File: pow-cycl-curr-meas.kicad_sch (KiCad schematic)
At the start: 86 parts, among them Q10 2N7002K-T1-E3, Q6 2N7002K-T1-E3, Q7 2N7002K-T1-E3, Q8 2N7002K-T1-E3, Q9 2N7002K-T1-E3, U10 TCA9534, U11 TMCS1100A2-Q1, U12 TMCS1100A2-Q1, U13 TMCS1100A2-Q1, U14 ADS7828, U8 TMCS1100A2-Q1, U9 TMCS1100A2-Q1

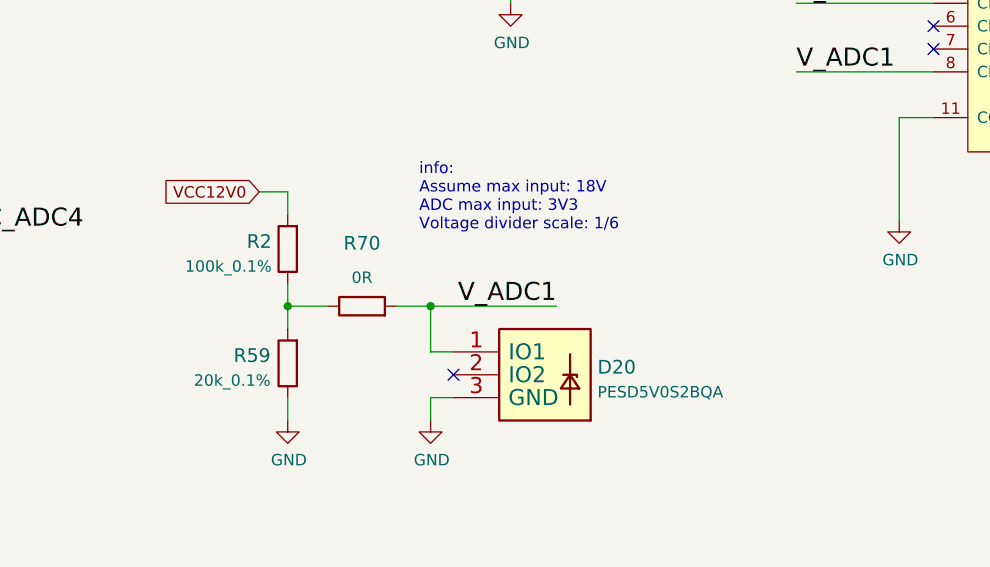
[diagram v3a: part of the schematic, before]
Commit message: Exchanged resistor in divider for voltage measurement
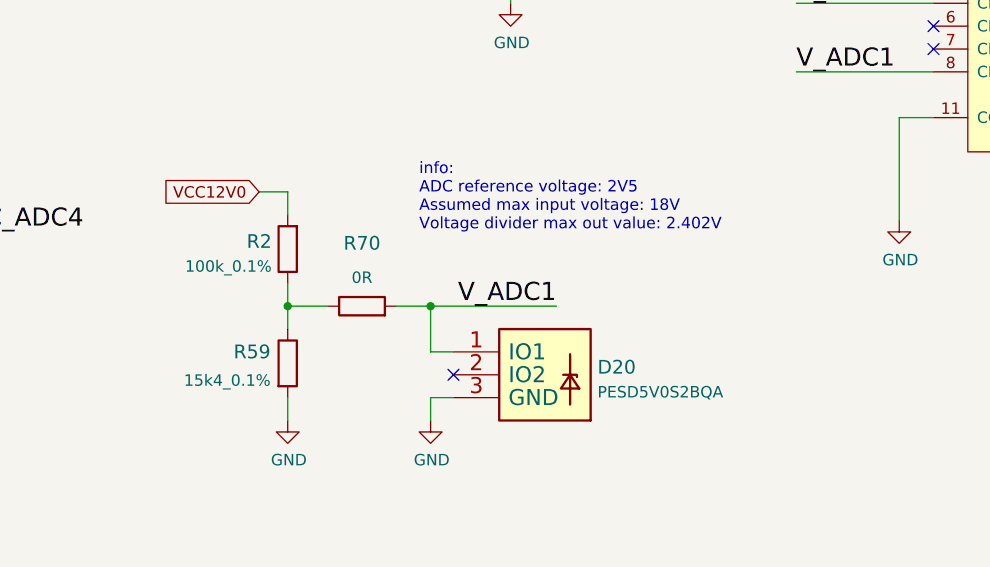
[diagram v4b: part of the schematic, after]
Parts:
- removed R59: R_20k_0.1%_0402, antmicro-footprints:0402-res, symbol antmicroResistors0402:R_20k_0.1%_0402
- added R59: R_15k4_0.1%_0402, antmicro-footprints:0402-res, symbol antmicroResistors0402:R_15k4_0.1%_0402
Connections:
- net GND: now also R59.2
- net at R2.1, R70.1: now also R59.1
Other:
- note added: "info: ADC reference voltage: 2V5 Assumed max input voltage: 18V Voltage divider max out value: 2.402V"
- note removed: "info: Assume max input: 18V ADC max input: 3V3 Voltage divider scale: 1/6"
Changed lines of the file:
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@@
     (effects (font (size 2.0066 2.0066)) (justify left bottom))
   )
-  (text "info:\nAssume max input: 18V\nADC max input: 3V3\nVoltage divider scale: 1/6"
+  (text "info:\nADC reference voltage: 2V5\nAssumed max input voltage: 18V\nVoltage divider max out value: 2.402V"
     (at 196.85 91.44 0)
     (effects (font (size 1.27 1.27)) (justify left bottom))
@@
     (pin "1")
   )
+  (symbol (lib_id "antmicroResistors0402:R_15k4_0.1%_0402") (at 182.245 106.045 270) (unit 1)
+    (in_bom yes) (on_board yes)
+    (property "Reference" "R59" (id 0) (at 180.34 104.7751 90)
+      (effects (font (size 1.524 1.524)) (justify right))
+    )
+    (property "Value" "R_15k4_0.1%_0402" (id 1) (at 174.625 106.045 0)
+      (effects (font (size 1.524 1.524)) hide)
+    )
+    (property "Footprint" "antmicro-footprints:0402-res" (id 2) (at 187.325 111.125 0)
+      (effects (font (size 1.524 1.524)) (justify left) hide)
+    )
+    (property "Datasheet" "https://www.mouser.pl/datasheet/2/315/AOA0000C307-1149632.pdf" (id 3) (at 177.165 106.045 0)
+      (effects (font (size 1.27 1.27)) hide)
+    )
+    (property "Manufacturer" "Panasonic" (id 4) (at 192.405 111.125 0)
+      (effects (font (size 1.524 1.524)) (justify left) hide)
+    )
+    (property "MPN" "ERA-2AEB1542X" (id 5) (at 189.865 111.125 0)
+      (effects (font (size 1.524 1.524)) (justify left) hide)
+    )
+    (property "Val" "15k4_0.1%" (id 6) (at 180.34 107.95 90)
+      (effects (font (size 1.27 1.27)) (justify right))
+    )
+    (pin "1")
+    (pin "2")
+  )
   (symbol (lib_id "antmicroTransistorsFETsMOSFETsSingle:2N7002K-T1-E3") (at 246.38 247.015 0) (unit 1)
     (in_bom yes) (on_board yes) (fields_autoplaced)
@@
     (pin "3")
   )
-  (symbol (lib_id "antmicroResistors0402:R_20k_0.1%_0402") (at 182.245 106.045 90) (unit 1)
-    (in_bom yes) (on_board yes)
-    (property "Reference" "R59" (id 0) (at 180.34 105.1849 90)
-      (effects (font (size 1.524 1.524)) (justify left))
-    )
-    (property "Value" "R_20k_0.1%_0402" (id 1) (at 187.325 106.045 0)
-      (effects (font (size 1.524 1.524)) hide)
-    )
-    (property "Footprint" "antmicro-footprints:0402-res" (id 2) (at 177.165 100.965 0)
-      (effects (font (size 1.524 1.524)) (justify left) hide)
-    )
-    (property "Datasheet" "https://www.mouser.pl/datasheet/2/447/PYu_RC_Group_51_RoHS_L_11-1984063.pdf" (id 3) (at 189.865 106.045 0)
-      (effects (font (size 1.27 1.27)) hide)
-    )
-    (property "Manufacturer" "Yageo" (id 4) (at 172.085 100.965 0)
-      (effects (font (size 1.524 1.524)) (justify left) hide)
-    )
-    (property "MPN" "RC0402BR-0720KL" (id 5) (at 174.625 100.965 0)
-      (effects (font (size 1.524 1.524)) (justify left) hide)
-    )
-    (property "Val" "20k_0.1%" (id 6) (at 180.34 107.95 90)
-      (effects (font (size 1.27 1.27)) (justify left))
-    )
-    (pin "1")
-    (pin "2")
-  )
   (symbol (lib_id "d1600e-psu-breakout-board:GND") (at 130.175 259.715 0) (unit 1)

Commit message: Fixed IO expander MPN
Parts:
- U10: MPN TCA9534ADWR -> TCA9534PWR
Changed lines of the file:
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@@
       (effects (font (size 1.27 1.27)) hide)
     )
-    (property "MPN" "TCA9534ADWR" (id 4) (at 83.82 185.42 0)
+    (property "MPN" "TCA9534PWR" (id 4) (at 83.82 185.42 0)
       (effects (font (size 1.27 1.27)) hide)
     )

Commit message: [#63472] Add OHP assets
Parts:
- removed C29, C30, C31, C32: C_100n_0402, d1600e-psu-breakout-board-footprints:0402-cap, symbol d1600e-psu-breakout-board:C_100n_0402
- removed D15, D16, D17, D18, D19: BZT52B15SV-T, antmicro-footprints:SOD-323, symbol antmicroDiodesZenerSingle:BZT52B15SV-T
- removed Q10, Q6, Q7, Q8, Q9: 2N7002K-T1-E3, antmicro-footprints:SOT-23-3, symbol antmicroTransistorsFETsMOSFETsSingle:2N7002K-T1-E3
- removed QA1, QA2, QA3, QA4, QA5, QB1, QB2, QB3, QB4, QB5: SI7613DN-T1-GE3, antmicro-footprints:Vishay_PowerPAK_1212-8_Single, symbol antmicroTransistorsFETsMOSFETsSingle:SI7613DN-T1-GE3
- removed R20, R21, R24, R26, R27, R46, R47, R48, R49, R50: R_10k_0402, d1600e-psu-breakout-board-footprints:0402-res, symbol d1600e-psu-breakout-board:R_10k_0402
- removed R22, R23, R25, R28, R29: R_4k7_0402, d1600e-psu-breakout-board-footprints:0402-res, symbol d1600e-psu-breakout-board:R_4k7_0402
- removed R60, R61, R62, R63, R64, R65, R66, R67, R68, R69: R_2R_0402, antmicro-footprints:0402-res, symbol antmicroResistors0402:R_2R_0402
- removed U11, U12, U13, U9: TMCS1100A2-Q1, d1600e-psu-breakout-board-footprints:SOIC-8_W3.9mm, symbol d1600e-psu-breakout-board:TMCS1100A2-Q1
- added C29, C30, C31, C32: C_100n_0402, antmicro-footprints:C_0402_1005Metric, symbol antmicroCapacitors0402:C_100n_0402
- added U11, U12, U13, U9: TMCS1100A2-Q1, antmicro-footprints:SOIC-8_3.9x4.9x1.75mm_P1.27mm, symbol antmicroPowerMeasurement:TMCS1100A2-Q1
- C21, C28, C37: footprint d1600e-psu-breakout-board-footprints:0402-cap -> antmicro-footprints:C_0402_1005Metric; symbol d1600e-psu-breakout-board:C_100n_0402 -> antmicroCapacitors0402:C_100n_0402; Author (none) -> Antmicro; Dielectric (none) -> X5R; License (none) -> Apache-2.0; Voltage (none) -> 50V
- C22: footprint d1600e-psu-breakout-board-footprints:0402-cap -> antmicro-footprints:C_0402_1005Metric; symbol d1600e-psu-breakout-board:C_1u_0402 -> antmicroCapacitors0402:C_1u_0402; Author (none) -> Antmicro; License (none) -> Apache-2.0
- D20: footprint d1600e-psu-breakout-board-footprints:TPD2E009DRTR -> antmicro-footprints:TPD2E009DRTR; symbol d1600e-psu-breakout-board:PESD5V0S2BQA -> antmicroTVSDiodes:PESD5V0S2BQA; Author (none) -> Antmicro; License (none) -> Apache-2.0
- FB4: value BLM18AG601SN1D -> FB_600Z_0.5A_Murata-BLM18AG_0603; footprint d1600e-psu-breakout-board-footprints:0603 -> antmicro-footprints:FB_0603_1608Metric; symbol d1600e-psu-breakout-board:BLM18AG601SN1D -> antmicroFerriteBeadsandChips:FB_600Z_0.5A_Murata-BLM18AG_0603; Author (none) -> Antmicro; DNP DNP -> (none); License (none) -> Apache-2.0; Manufacturer Murata Electronics North America -> Murata; Val (none) -> 600Z/0.5A
- R13, R15, R30, R32: footprint d1600e-psu-breakout-board-footprints:0402-res -> antmicro-footprints:R_0402_1005Metric; symbol d1600e-psu-breakout-board:R_0R_0402 -> antmicroResistors0402:R_0R_0402; Author (none) -> Antmicro; Current (none) -> 1A; License (none) -> Apache-2.0; Manufacturer PANASONIC -> Panasonic; now not fitted; now left out of the parts list
- R14, R16, R18, R31, R33, R70: footprint d1600e-psu-breakout-board-footprints:0402-res -> antmicro-footprints:R_0402_1005Metric; symbol d1600e-psu-breakout-board:R_0R_0402 -> antmicroResistors0402:R_0R_0402; Author (none) -> Antmicro; Current (none) -> 1A; License (none) -> Apache-2.0; Manufacturer PANASONIC -> Panasonic
- R17: footprint d1600e-psu-breakout-board-footprints:0402-res -> antmicro-footprints:R_0402_1005Metric; symbol d1600e-psu-breakout-board:R_0R_0402 -> antmicroResistors0402:R_0R_0402; Author (none) -> Antmicro; Current (none) -> 1A; DNP DNP` -> DNP; License (none) -> Apache-2.0; Manufacturer PANASONIC -> Panasonic; now not fitted; now left out of the parts list
- R19: footprint d1600e-psu-breakout-board-footprints:0402-res -> antmicro-footprints:R_0402_1005Metric; symbol d1600e-psu-breakout-board:R_4k7_0402 -> antmicroResistors0402:R_4k7_0402; Author (none) -> Antmicro; License (none) -> Apache-2.0; MPN MCS04020C4701FE000 -> CR0402-FX-4701GLF; Manufacturer VISHAY -> Bourns; Tolerance (none) -> 1%
- R2: footprint antmicro-footprints:0402-res -> antmicro-footprints:R_0402_1005Metric; Author (none) -> Antmicro; License (none) -> Apache-2.0; Tolerance (none) -> 0.1%; Val 100k_0.1% -> 100k
- R59: footprint antmicro-footprints:0402-res -> antmicro-footprints:R_0402_1005Metric; Author (none) -> Antmicro; License (none) -> Apache-2.0; Tolerance (none) -> 0.1%; Val 15k4_0.1% -> 15k4
- TP_ADC1, TP_ADC2, TP_ADC3, TP_ADC4, TP_ADC5, TP_PC1, TP_PC2, TP_PC3, TP_PC4, TP_PC5: value TP_SMD1MM -> TP_1mm_SMD; footprint d1600e-psu-breakout-board-footprints:Testpoint_smd_1mm -> antmicro-footprints:TP_SMD_1mm; symbol d1600e-psu-breakout-board:TP_SMD1MM -> antmicroTestPoints:TP_1mm_SMD; Author (none) -> Antmicro; License (none) -> Apache-2.0; now left out of the parts list
- U10: value TCA9534 -> TCA9534PWR_TSSOP; footprint d1600e-psu-breakout-board-footprints:TSSOP-16 -> antmicro-footprints:TSSOP-16_4.4x5mm_P0.65mm; symbol d1600e-psu-breakout-board:TCA9534 -> antmicroInterfaceIOExpanders:TCA9534PWR_TSSOP; Author (none) -> Antmicro; License (none) -> Apache-2.0; Manufaacturer Texas Instruments -> (none)
- U14: footprint d1600e-psu-breakout-board-footprints:TSSOP-16_4.4x5mm_P0.65mm -> antmicro-footprints:TSSOP-16_4.4x5mm_P0.65mm; symbol d1600e-psu-breakout-board:ADS7828 -> antmicroDataAcquisitionAnalogtoDigitalConvertersADC:ADS7828; Author (none) -> Antmicro; License (none) -> Apache-2.0; MPN ADS7828E/250 -> ADS7828E/250
- U8: footprint d1600e-psu-breakout-board-footprints:SOIC-8_W3.9mm -> antmicro-footprints:SOIC-8_3.9x4.9x1.75mm_P1.27mm; symbol d1600e-psu-breakout-board:TMCS1100A2-Q1 -> antmicroPowerMeasurement:TMCS1100A2-Q1; Author (none) -> Antmicro; License (none) -> Apache-2.0
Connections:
- net C_ADC2: now also U9.7 (VOUT)
- net C_ADC3: now also U11.7 (VOUT)
- net C_ADC4: now also U12.7 (VOUT)
- net C_ADC5: now also U13.7 (VOUT)
- net C_MEAS_2: now also U9.1 (IN+), U9.2 (IN+)
- net C_MEAS_3: now also U11.1 (IN+), U11.2 (IN+)
- net C_MEAS_4: now also U12.1 (IN+), U12.2 (IN+)
- net C_MEAS_5: now also U13.1 (IN+), U13.2 (IN+)
- net GND: now also C21.1, C22.1, C37.1, C29.2, C30.2, C31.2, C32.2, U11.5 (GND), U11.6 (VREF), U12.5 (GND), U12.6 (VREF), U13.5 (GND), U13.6 (VREF), U9.5 (GND), U9.6 (VREF); no longer C21.2, C22.2, C37.2
- net LOAD_2: now also U9.3 (IN-), U9.4 (IN-)
- net LOAD_3: now also U11.3 (IN-), U11.4 (IN-)
- net LOAD_4: now also U12.3 (IN-), U12.4 (IN-)
- net LOAD_5: now also U13.3 (IN-), U13.4 (IN-)
- net VCC3V3: now also C21.2, C22.2, C29.1, C30.1, C31.1, C32.1, U11.8 (VCC), U12.8 (VCC), U13.8 (VCC), U9.8 (VCC); no longer C21.1, C22.1
- net at FB4.2, U14.10 (REF): now also C37.2; no longer C37.1
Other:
- added sheet Power switch 1 (power-switch.kicad_sch)
- added sheet Power switch 2 (power-switch.kicad_sch)
- added sheet Power switch 3 (power-switch.kicad_sch)
- added sheet Power switch 4 (power-switch.kicad_sch)
- added sheet Power switch 5 (power-switch.kicad_sch)
- note added: "Hall-Effect current sensors"
- note removed: "HALL SENSORS"
- note removed: "Power filtration"
- note removed: "Sensors"
- note removed: "Supply"
- note removed: "UP TO 15A"
- moved on the sheet: C21, C22, C28, C37, D20, R14, R16, R18, R19, R2, R31, R33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
